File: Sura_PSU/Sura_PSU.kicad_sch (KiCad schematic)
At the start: 16 parts, among them J1 12VDC In, J2 X11, J3 X11, U1 PSU2-5, U2 NKE1212SC

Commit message: Initial commit (to be tested)
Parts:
- removed J1: 12VDC In, Connector_JST:JST_VH_B2P-VH_1x02_P3.96mm_Vertical, symbol Connector_Generic:Conn_01x02
- added J1: 12V In, Clueless_Engineer:694106301002, symbol Connector:Barrel_Jack_MountingPin
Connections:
- net GND: now also J1.2, J1.3 (MountPin)
- net at F1.1: now also J1.1
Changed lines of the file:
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@@
+	)
+	(junction
+		(at 50.8 73.66)
+		(diameter 0)
+		(color 0 0 0 0)
 	)
 	(junction
@@
 	(wire
 		(pts
+			(xy 50.8 73.66) (xy 50.8 78.74)
+		)
+		(stroke
+			(width 0)
+			(type default)
+		)
+	)
+	(wire
+		(pts
 			(xy 201.93 52.07) (xy 152.4 52.07)
 		)
@@
 	(wire
 		(pts
+			(xy 43.18 78.74) (xy 50.8 78.74)
+		)
+		(stroke
+			(width 0)
+			(type default)
+		)
+	)
+	(wire
+		(pts
 			(xy 93.98 87.63) (xy 109.22 87.63)
 		)
@@
 		(pts
 			(xy 215.9 87.63) (xy 215.9 71.12)
+		)
+		(stroke
+			(width 0)
+			(type default)
+		)
+	)
+	(wire
+		(pts
+			(xy 50.8 71.12) (xy 50.8 73.66)
 		)
 		(stroke
@@
 			)
 			(justify left bottom)
+		)
+	)
+	(symbol
+		(lib_id "Connector:Barrel_Jack_MountingPin")
+		(at 43.18 71.12 0)
+		(unit 1)
+		(exclude_from_sim no)
+		(in_bom yes)
+		(on_board yes)
+		(dnp no)
+		(fields_autoplaced yes)
+		(property "Reference" "J1"
+			(at 43.18 62.23 0)
+			(effects
+				(font
+					(size 1.27 1.27)
+				)
+			)
+		)
+		(property "Value" "12V In"
+			(at 43.18 64.77 0)
+			(effects
+				(font
+					(size 1.27 1.27)
+				)
+			)
+		)
+		(property "Footprint" "Clueless_Engineer:694106301002"
+			(at 44.45 72.136 0)
+			(effects
+				(font
+					(size 1.27 1.27)
+				)
+				(hide yes)
+			)
+		)
+		(property "Datasheet" "~"
+			(at 44.45 72.136 0)
+			(effects
+				(font
+					(size 1.27 1.27)
+				)
+				(hide yes)
+			)
+		)
+		(property "Description" "DC Barrel Jack with a mounting pin"
+			(at 43.18 71.12 0)
+			(effects
+				(font
+					(size 1.27 1.27)
+				)
+				(hide yes)
+			)
+		)
+		(pin "3"
+		)
+		(pin "1"
+		)
+		(pin "2"
+		)
+		(instances
+			(project "Sura_PSU"
+				(path "/ad1c8779-1df4-4d72-a3dd-3e94406ac526"
+					(reference "J1")
+					(unit 1)
+				)
+			)
 		)
 	)
@@
 					(unit 1)
 				)
-			)
-		)
-	)
-	(symbol
-		(lib_id "Connector_Generic:Conn_01x02")
-		(at 45.72 71.12 180)
-		(unit 1)
-		(exclude_from_sim no)
-		(in_bom yes)
-		(on_board yes)
-		(dnp no)
-		(fields_autoplaced yes)
-		(property "Reference" "J1"
-			(at 45.72 62.23 0)
-			(effects
-				(font
-					(size 1.27 1.27)
-				)
-			)
-		)
-		(property "Value" "12VDC In"
-			(at 45.72 64.77 0)
-			(effects
-				(font
-					(size 1.27 1.27)
-				)
-			)
-		)
-		(property "Footprint" "Connector_JST:JST_VH_B2P-VH_1x02_P3.96mm_Vertical"
-			(at 45.72 71.12 0)
-			(effects
-				(font
-					(size 1.27 1.27)
-				)
-				(hide yes)
-			)
-		)
-		(property "Datasheet" "~"
-			(at 45.72 71.12 0)
-			(effects
-				(font
-					(size 1.27 1.27)
-				)
-				(hide yes)
-			)
-		)
-		(property "Description" "Generic connector, single row, 01x02, script generated (kicad-library-utils/schlib/autogen/connector/)"
-			(at 45.72 71.12 0)
-			(effects
-				(font
-					(size 1.27 1.27)
-				)
-				(hide yes)
-			)
-		)
-		(pin "1"
-		)
-		(pin "2"
-		)
-		(instances
-			(project "Sura_PSU"
-				(path "/ad1c8779-1df4-4d72-a3dd-3e94406ac526"
-					(reference "J1")
-					(unit 1)
-				)

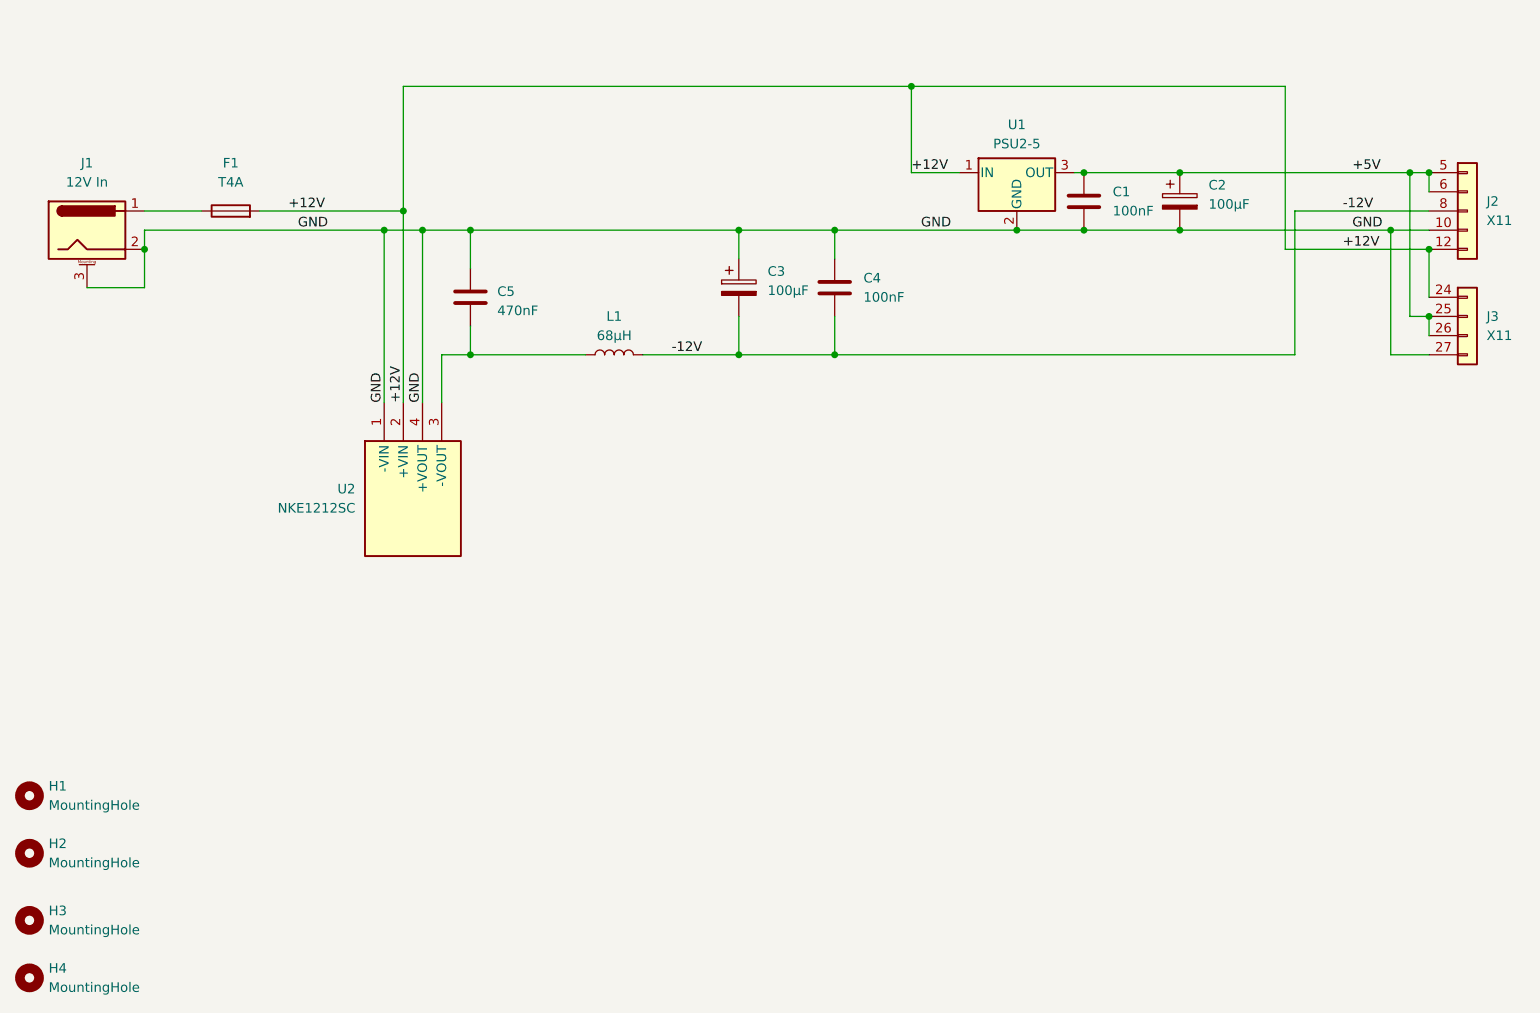
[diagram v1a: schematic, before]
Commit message: Updated design (swapped 5V regulator)
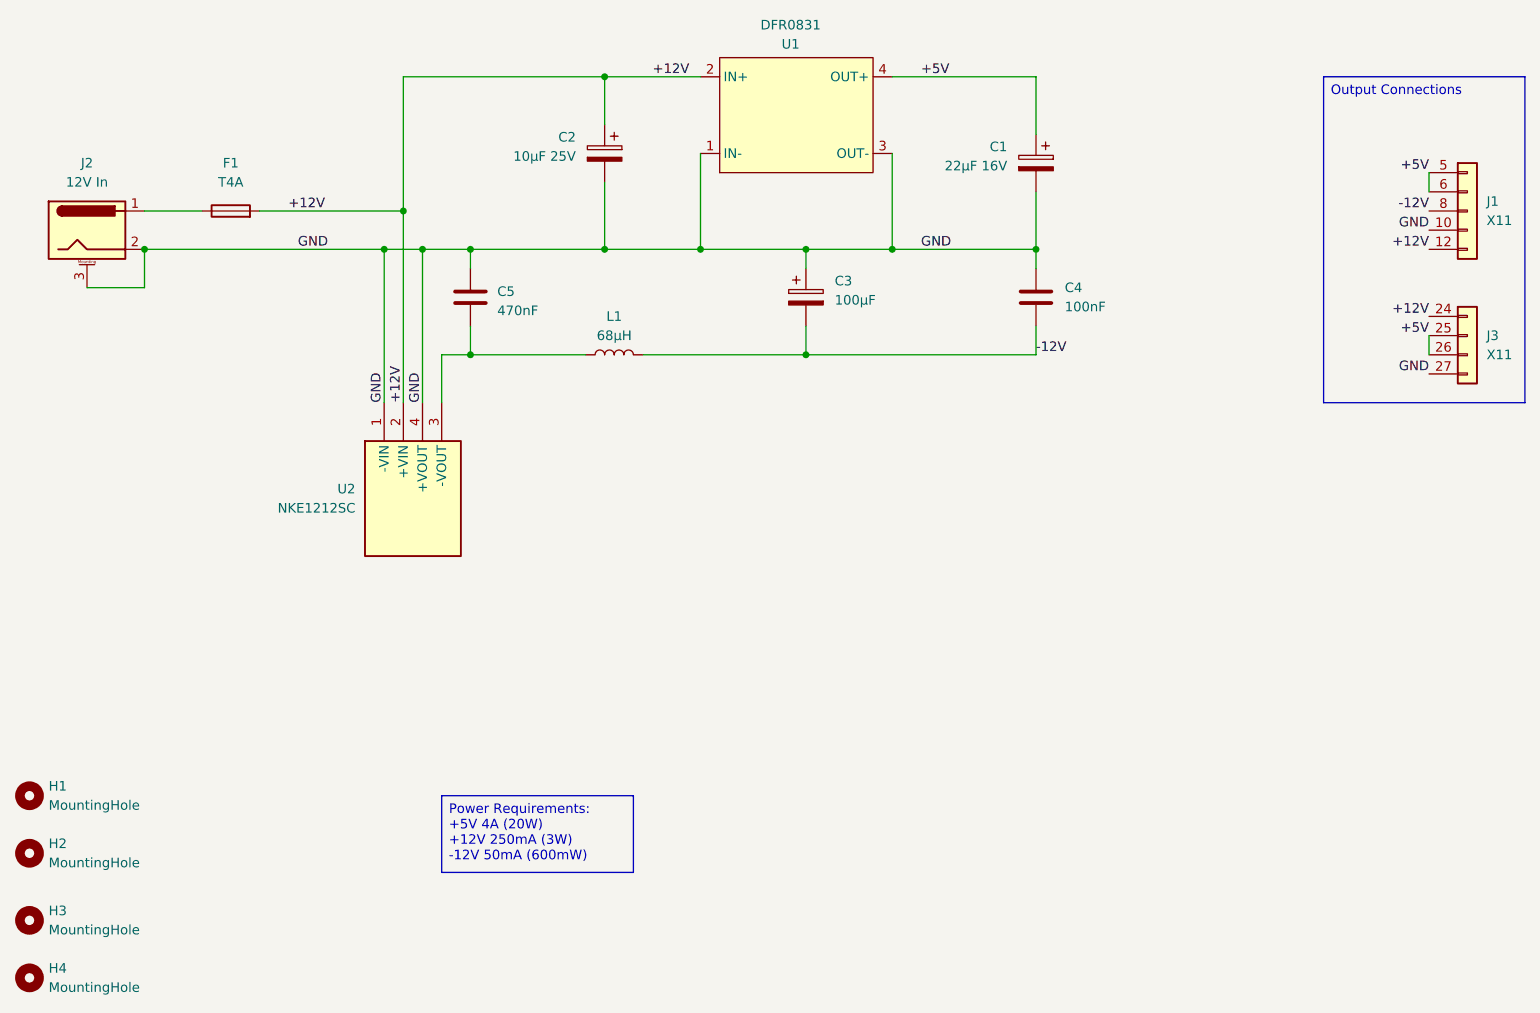
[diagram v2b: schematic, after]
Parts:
- removed C1: 100nF, Capacitor_THT:C_Disc_D3.4mm_W2.1mm_P2.50mm, symbol Device:C
- removed U1: PSU2-5, Package_TO_SOT_THT:TO-220-3_Horizontal_TabDown, symbol Regulator_Linear:L7805
- added C1: 22µF 16V, Capacitor_THT:CP_Radial_D5.0mm_P2.50mm, symbol Device:C_Polarized
- added U1: DFR0831, Clueless_Engineer:DFR0831, symbol Clueless_Engineer:DFR0831
- C2: value 100µF -> 10µF 25V
- renumbered J2 to J1, J1 to J2
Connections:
- net +12V: now also C2.1, U1.2 (IN+)
- net +5V: now also C1.1, U1.4 (OUT+); no longer C2.1
- net GND: now also C1.2, U1.1 (IN-), U1.3 (OUT-)
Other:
- moved on the sheet: C3, C4, J3
